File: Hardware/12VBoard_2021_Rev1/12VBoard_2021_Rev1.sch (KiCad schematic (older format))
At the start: 0 parts

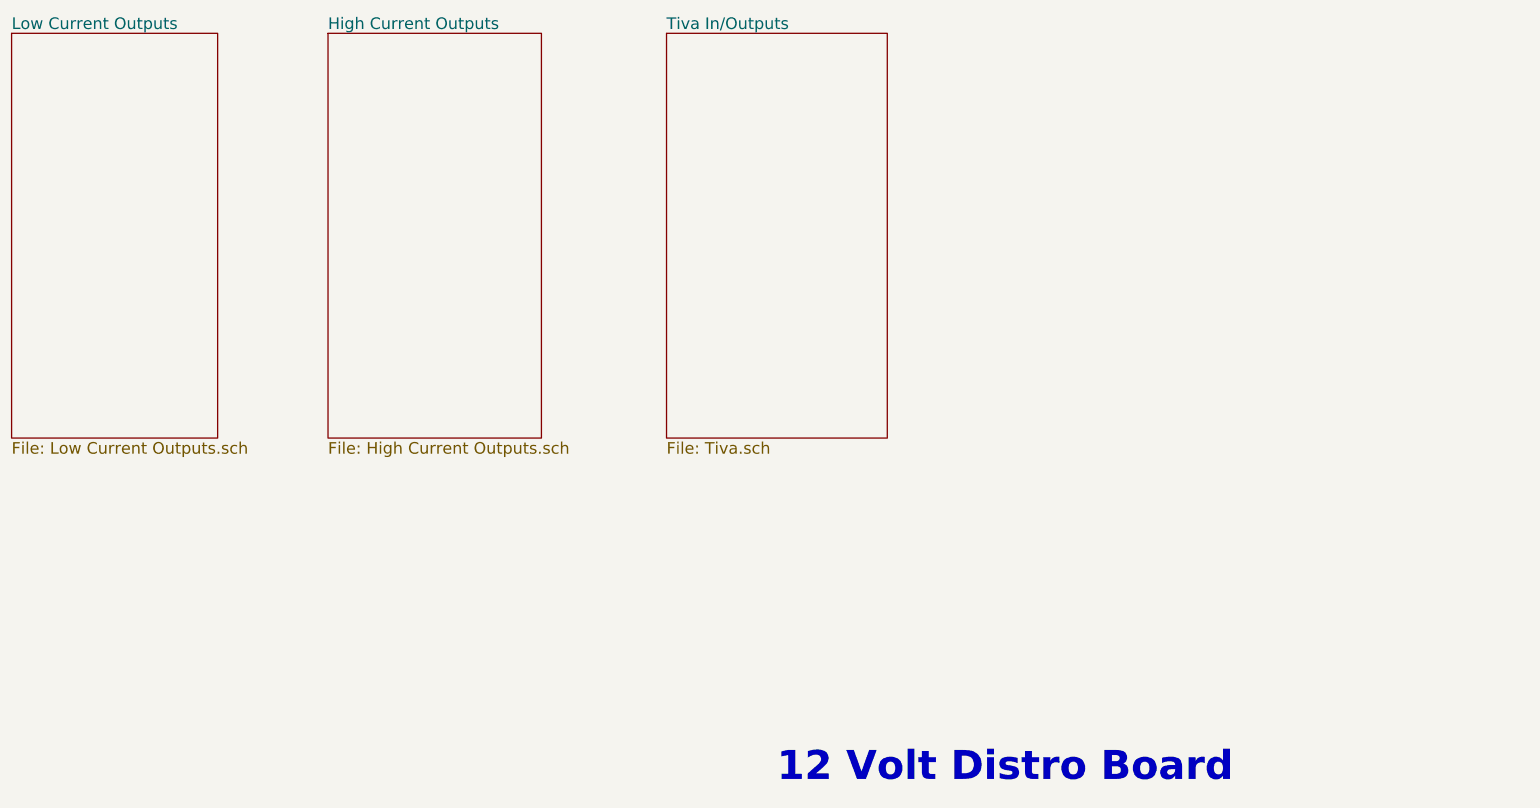
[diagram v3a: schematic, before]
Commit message: Created Buck Circuts
added boxes that Dan hates
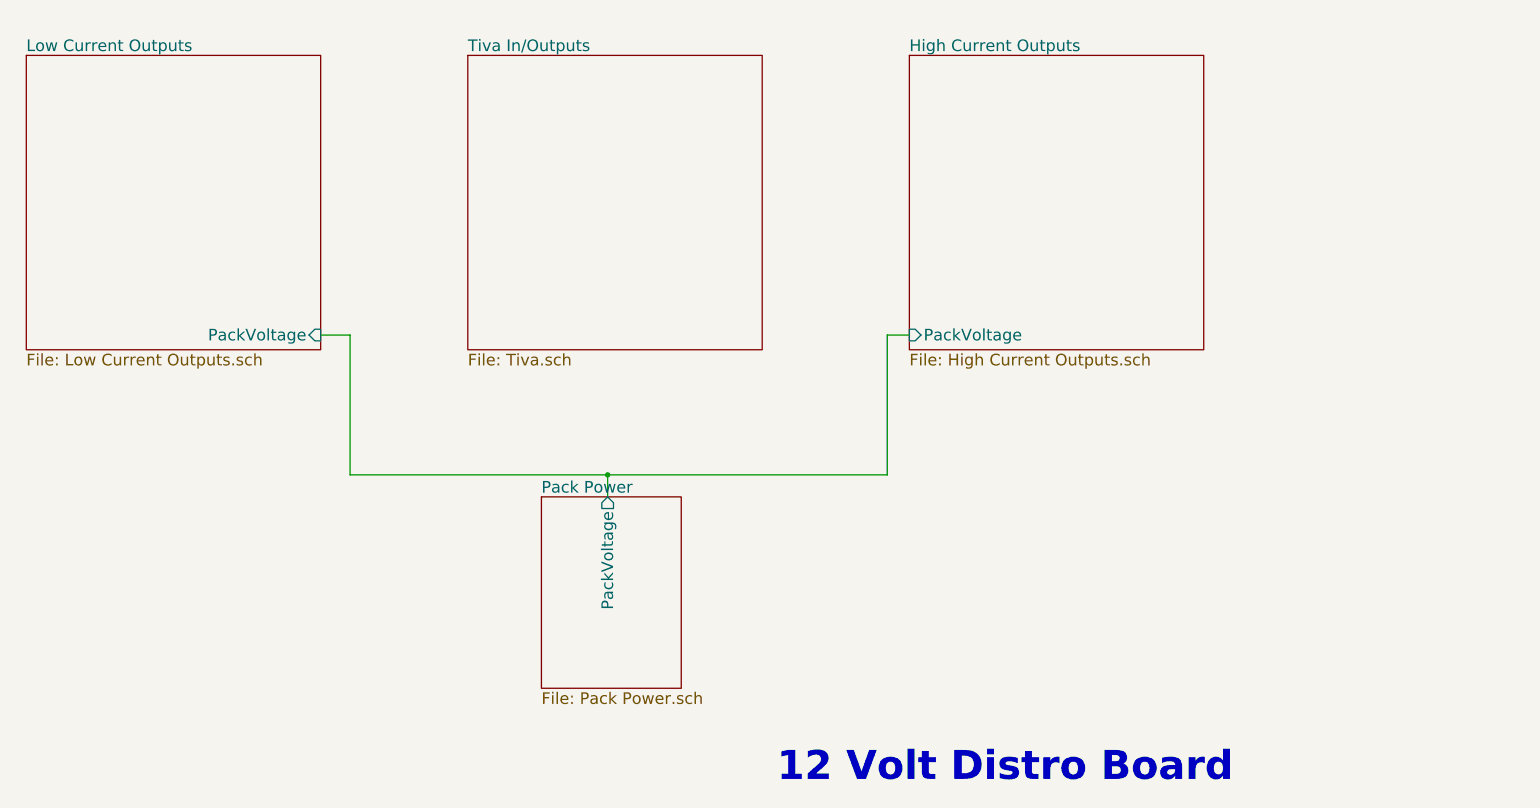
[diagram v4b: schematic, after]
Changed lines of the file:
@@
 $Descr A4 11693 8268
 encoding utf-8
-Sheet 1 4
+Sheet 1 10
 Title ""
 Date ""
@@
 12 Volt Distro Board
 $Sheet
-S 1900 1850 1400 2750
-U 5F74F223
-F0 "Low Current Outputs" 79
-F1 "Low Current Outputs.sch" 79
-$EndSheet
-$Sheet
-S 4050 1850 1450 2750
-U 5F74F36B
-F0 "High Current Outputs" 79
-F1 "High Current Outputs.sch" 79
-$EndSheet
-$Sheet
-S 6350 1850 1500 2750
+S 5000 2000 2000 2000
 U 5F74F4A3
 F0 "Tiva In/Outputs" 79
 F1 "Tiva.sch" 79
 $EndSheet
+$Sheet
+S 5500 5000 950  1300
+U 5F8031F1
+F0 "Pack Power" 79
+F1 "Pack Power.sch" 79
+F2 "PackVoltage" O T 5950 5000 79
+$EndSheet
+Wire Wire Line
+	5950 5000 5950 4850
+Wire Wire Line
+	5950 4850 7850 4850
+Connection ~ 5950 4850
+Wire Wire Line
+	4200 4850 5950 4850
+Wire Wire Line
+	4200 3900 4200 4850
+Wire Wire Line
+	4000 3900 4200 3900
+Wire Wire Line
+	7850 4850 7850 3900
+Wire Wire Line
+	7850 3900 8000 3900
+$Sheet
+S 8000 2000 2000 2000
+U 5F74F36B
+F0 "High Current Outputs" 79
+F1 "High Current Outputs.sch" 79
+F2 "PackVoltage" I L 8000 3900 79
+$EndSheet
+$Sheet
+S 2000 2000 2000 2000
+U 5F74F223
+F0 "Low Current Outputs" 79
+F1 "Low Current Outputs.sch" 79
+F2 "PackVoltage" I R 4000 3900 79
+$EndSheet
 $EndSCHEMATC

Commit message: Ferite bead?
MERGE?????
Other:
- note added: "12 Volt 'THE Distro' Board"
- note removed: "12 Volt Distro Board"
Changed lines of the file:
@@
 $Descr A4 11693 8268
 encoding utf-8
-Sheet 1 13
+Sheet 1 8
 Title ""
 Date ""
@@
 $EndDescr
 Text Notes 7100 6950 0    197  ~ 39
-12 Volt Distro Board
+12 Volt 'THE Distro' Board
 $Sheet
 S 5000 2000 2000 2000
@@
 F0 "Tiva In/Outputs" 79
 F1 "Tiva.sch" 79
+F2 "DriveSense" I R 7000 2125 79
+F3 "GimbalCTL" I L 5000 2375 79
+F4 "LowCurrentSense" I L 5000 2125 79
+F5 "AuxMountSense" I R 7000 2250 79
+F6 "CameraCTL" I L 5000 2250 79
+F7 "MultimediaSense" I R 7000 2375 79
+F8 "NavBoardCTL" I L 5000 2500 79
+F9 "AuxCTL" I R 7000 2500 79
+F10 "MultimediaSense" I R 7000 2625 79
 $EndSheet
 $Sheet
@@
 F1 "Pack Power.sch" 79
 F2 "PackVoltage" O T 5950 5000 79
+F3 "5V" O T 6150 5000 79
 $EndSheet
 Wire Wire Line
@@
 	7850 3900 8000 3900
 $Sheet
+S 2000 2000 2000 2000
+U 5F74F223
+F0 "Low Current Outputs" 79
+F1 "Low Current Outputs.sch" 79
+F2 "PackVoltage" I R 4000 3900 79
+F3 "5V" I R 4000 3625 79
+F4 "CameraToggle" I R 4000 2250 79
+F5 "GimbalToggle" I R 4000 2375 79
+F6 "NavToggle" I R 4000 2500 79
+F7 "CurrentSense" I R 4000 2125 79
+$EndSheet
+Wire Wire Line
+	6150 5000 6150 4525
+Wire Wire Line
+	6150 4525 4525 4525
+Wire Wire Line
+	4525 4525 4525 3625
+Wire Wire Line
+	4525 3625 4000 3625
+Wire Wire Line
+	6150 4525 7525 4525
+Connection ~ 6150 4525
+Wire Wire Line
+	7525 3625 8000 3625
+Wire Wire Line
+	7525 3625 7525 4525
+$Sheet
 S 8000 2000 2000 2000
 U 5F74F36B
@@
 F1 "High Current Outputs.sch" 79
 F2 "PackVoltage" I L 8000 3900 79
+F3 "5V" I L 8000 3625 79
 $EndSheet
-$Sheet
-S 2000 2000 2000 2000
-U 5F74F223
-F0 "Low Current Outputs" 79
-F1 "Low Current Outputs.sch" 79
-F2 "PackVoltage" I R 4000 3900 79
-$EndSheet
+Wire Wire Line
+	5000 2250 4000 2250
+Wire Wire Line
+	5000 2375 4000 2375
+Wire Wire Line
+	4000 2500 5000 2500
+Wire Wire Line
+	5000 2125 4000 2125
 $EndSCHEMATC

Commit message: High current
Fisnished adding labes/tags
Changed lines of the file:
@@
 F0 "Tiva In/Outputs" 79
 F1 "Tiva.sch" 79
-F2 "DriveSense" I R 7000 2125 79
-F3 "GimbalCTL" I L 5000 2375 79
+F2 "DriveSense" I R 7000 2150 79
+F3 "GimbalCTL" O L 5000 2375 79
 F4 "LowCurrentSense" I L 5000 2125 79
 F5 "AuxMountSense" I R 7000 2250 79
-F6 "CameraCTL" I L 5000 2250 79
-F7 "MultimediaSense" I R 7000 2375 79
-F8 "NavBoardCTL" I L 5000 2500 79
-F9 "AuxCTL" I R 7000 2500 79
-F10 "MultimediaSense" I R 7000 2625 79
+F6 "CameraCTL" O L 5000 2250 79
+F7 "MultimediaSense" I R 7000 2350 79
+F8 "NavBoardCTL" O L 5000 2500 79
+F9 "AuxCTL" O R 7000 2450 79
+F10 "MultimediaCTL" O R 7000 2550 79
 $EndSheet
 $Sheet
@@
 F5 "GimbalToggle" I R 4000 2375 79
 F6 "NavToggle" I R 4000 2500 79
-F7 "CurrentSense" I R 4000 2125 79
+F7 "CurrentSense" O R 4000 2125 79
 $EndSheet
 Wire Wire Line
@@
 F2 "PackVoltage" I L 8000 3900 79
 F3 "5V" I L 8000 3625 79
+F4 "DriveSense" O L 8000 2150 79
+F5 "AuxMountSense" O L 8000 2250 79
+F6 "MultimediaSense" O L 8000 2350 79
+F7 "AuxCTL" I L 8000 2450 79
+F8 "MultimediaCTL" I L 8000 2550 79
 $EndSheet
 Wire Wire Line
@@
 Wire Wire Line
 	5000 2125 4000 2125
+Wire Wire Line
+	7000 2150 8000 2150
+Wire Wire Line
+	7000 2250 8000 2250
+Wire Wire Line
+	7000 2350 8000 2350
+Wire Wire Line
+	7000 2450 8000 2450
+Wire Wire Line
+	7000 2550 8000 2550
 $EndSCHEMATC

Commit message: reviewed
review
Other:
- note added: "12 Volt 'THE DISTRO' Board"
- note removed: "12 Volt 'THE Distro' Board"
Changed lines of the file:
@@
 $Descr A4 11693 8268
 encoding utf-8
-Sheet 1 8
+Sheet 1 7
 Title ""
 Date ""
@@
 Comment4 ""
 $EndDescr
-Text Notes 7100 6950 0    197  ~ 39
-12 Volt 'THE Distro' Board
+Text Notes 7025 6950 0    197  ~ 39
+12 Volt 'THE DISTRO' Board
 $Sheet
 S 5000 2000 2000 2000
